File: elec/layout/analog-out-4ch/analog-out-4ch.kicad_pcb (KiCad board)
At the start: 2 copper layers, 15 parts, among them U1 240kΩ ±1% 62.5mW, U10 100nF ±10% 16V X7R, U2 33kΩ ±1% 62.5mW, U3 240kΩ ±1% 62.5mW, U4 33kΩ ±1% 62.5mW, U5 240kΩ ±1% 62.5mW, U6 33kΩ ±1% 62.5mW, U7 240kΩ ±1% 62.5mW, U8 33kΩ ±1% 62.5mW

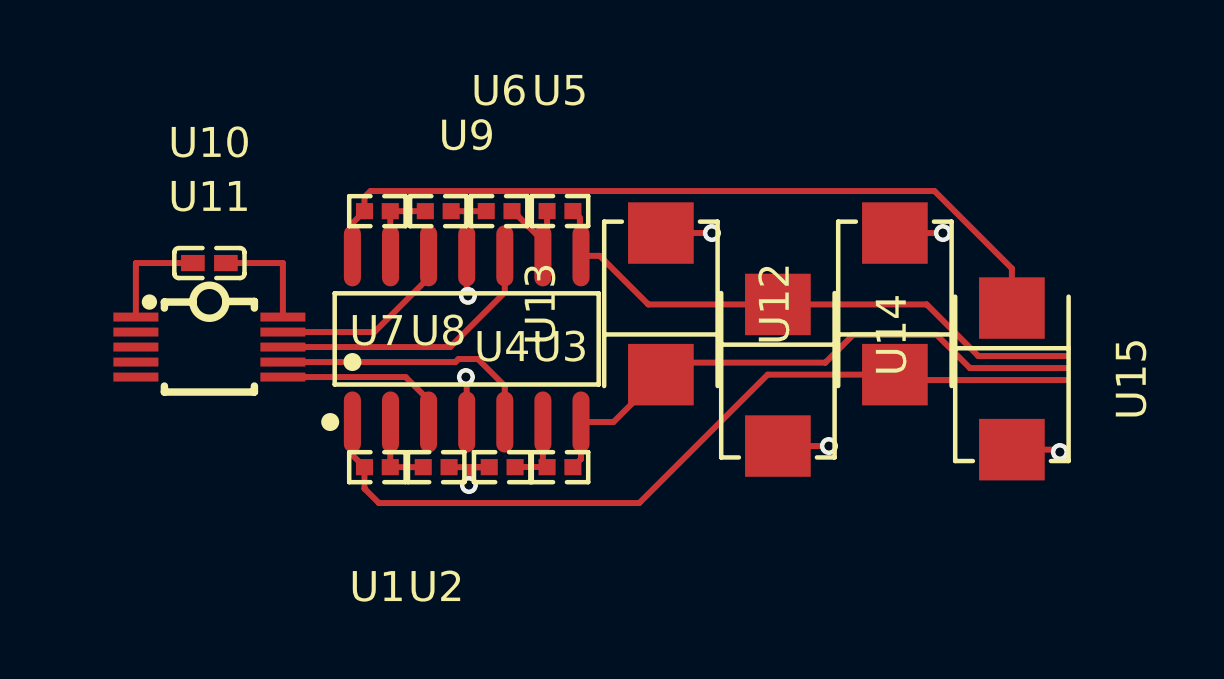
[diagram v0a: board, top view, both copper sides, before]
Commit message: fix short in thermistor design
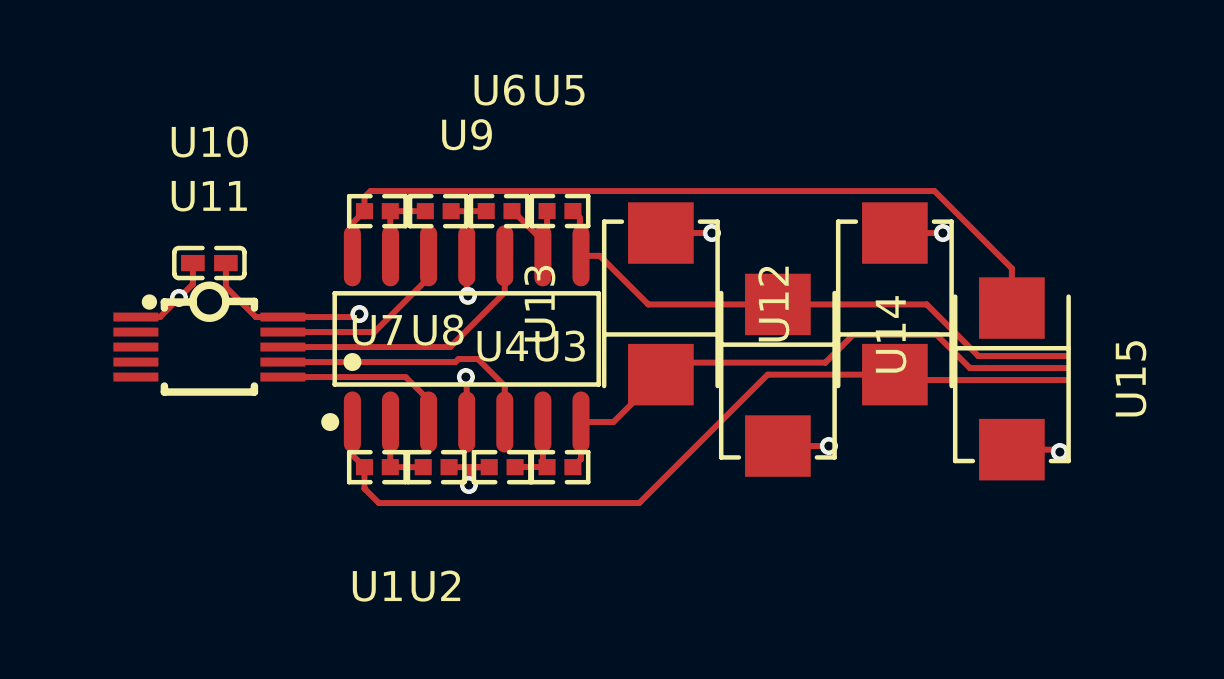
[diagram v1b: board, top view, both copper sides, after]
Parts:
- U1, U3, U5, U7: value 240kΩ ±1% 62.5mW -> 100Ω ±1% 62.5mW
- U2, U4, U6, U8: value 33kΩ ±1% 62.5mW -> 100Ω ±1% 62.5mW
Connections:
- U1 pad 2: line-4 -> line-6
- U10 pad 1: hv-1 -> hv
- U11 pad 1: hv-1 -> hv
- U11 pad 2: line-9 -> line-5
- U11 pad 6: line-7 -> line-9
- U11 pad 7: line-2 -> line-7
- U11 pad 8: line-6 -> line-4
- U11 pad 9: line-5 -> line-8
- U12 pad 1: line-4 -> line-6
- U12 pad 2: gnd-1 -> gnd
- U13 pad 1: line-1 -> line-2
- U13 pad 2: gnd-1 -> gnd
- U14 pad 1: line-8 -> line-1
- U14 pad 2: gnd-1 -> gnd
- U15 pad 2: gnd-1 -> gnd
- U2 pad 1: gnd-1 -> gnd
- U3 pad 2: line-1 -> line-2
- U4 pad 1: gnd-1 -> gnd
- U5 pad 2: line-8 -> line-1
- U6 pad 1: gnd-1 -> gnd
- U8 pad 1: gnd-1 -> gnd
- U9 pad 1: line-4 -> line-6
- U9 pad 10: line-6 -> line-4
- U9 pad 11: gnd-1 -> gnd
- U9 pad 12: line-5 -> line-8
- U9 pad 3: line-7 -> line-9
- U9 pad 4: hv -> hv-1
- U9 pad 5: line-2 -> line-7
- U9 pad 7: line-1 -> line-2
- U9 pad 8: line-8 -> line-1
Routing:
- net line-6: track 9.37 -> 28.3 mm
- net line-4: track 28.3 -> 9.37 mm
- net gnd: track 3.80 -> 20.6 mm, vias 0 -> 7
- net gnd-1: track 14.8 -> 0.00 mm, vias 6 -> 0
- net line-8: track 19.2 -> 6.34 mm
- net line-2: track 9.01 -> 19.9 mm
- net line-5: track 6.34 -> 0.00 mm
- net line-9: track 0.00 -> 5.91 mm
- net line-7: track 5.91 -> 9.01 mm
- net hv-1: track 3.70 -> 1.51 mm, vias 0 -> 1
- net hv: track 1.51 -> 3.06 mm
- net line-1: track 19.9 -> 19.2 mm

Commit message: update layouts to kicad 9
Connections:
- U1 pad 2: line-6 -> line-7
- U11 pad 2: line-5 -> line
- U11 pad 3: line -> line-2
- U11 pad 6: line-9 -> line-4
- U11 pad 7: line-7 -> line-6
- U11 pad 8: line-4 -> line-9
- U11 pad 9: line-8 -> line-1
- U12 pad 1: line-6 -> line-7
- U13 pad 1: line-2 -> line-3
- U14 pad 1: line-1 -> line-5
- U15 pad 1: line-3 -> line-8
- U3 pad 2: line-2 -> line-3
- U5 pad 2: line-1 -> line-5
- U7 pad 2: line-3 -> line-8
- U9 pad 1: line-6 -> line-7
- U9 pad 10: line-4 -> line-9
- U9 pad 12: line-8 -> line-1
- U9 pad 14: line-3 -> line-8
- U9 pad 3: line-9 -> line-4
- U9 pad 5: line-7 -> line-6
- U9 pad 7: line-2 -> line-3
- U9 pad 8: line-1 -> line-5
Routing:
- net line-8: track 6.34 -> 26.7 mm
- net line-2: track 19.9 -> 0.00 mm
- net line-7: track 9.01 -> 28.3 mm
- net line-6: track 28.3 -> 9.01 mm
- net line-5: track 0.00 -> 19.2 mm
- net line-1: track 19.2 -> 6.34 mm
- net line-3: track 26.7 -> 19.9 mm
- net line-9: track 5.91 -> 9.37 mm
- net line-4: track 9.37 -> 5.91 mm

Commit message: update LED gpio pin
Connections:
- U1 pad 2: line-7 -> line
- U11 pad 2: line -> line-2
- U11 pad 3: line-2 -> line-9
- U11 pad 6: line-4 -> line-3
- U11 pad 7: line-6 -> line-8
- U11 pad 8: line-9 -> line-5
- U12 pad 1: line-7 -> line
- U13 pad 1: line-3 -> line-4
- U14 pad 1: line-5 -> line-7
- U15 pad 1: line-8 -> line-6
- U3 pad 2: line-3 -> line-4
- U5 pad 2: line-5 -> line-7
- U7 pad 2: line-8 -> line-6
- U9 pad 1: line-7 -> line
- U9 pad 10: line-9 -> line-5
- U9 pad 14: line-8 -> line-6
- U9 pad 3: line-4 -> line-3
- U9 pad 5: line-6 -> line-8
- U9 pad 7: line-3 -> line-4
- U9 pad 8: line-5 -> line-7
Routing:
- net line: track 0.00 -> 28.3 mm
- net line-8: track 26.7 -> 9.01 mm
- net line-6: track 9.01 -> 26.7 mm
- net line-4: track 5.91 -> 19.9 mm
- net line-3: track 19.9 -> 5.91 mm
- net line-5: track 19.2 -> 9.37 mm
- net line-9: track 9.37 -> 0.00 mm
- net line-7: track 28.3 -> 19.2 mm
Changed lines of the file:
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@@
     )
     (net 0 "")
-    (net 1 "line-2")
-    (net 2 "line-4")
+    (net 1 "line-9")
+    (net 2 "line-3")
     (net 3 "hv")
     (net 4 "IN1_")
@@
     (net 7 "IN2_")
     (net 8 "IN3_")
-    (net 9 "line-6")
-    (net 10 "line-9")
+    (net 9 "line-8")
+    (net 10 "line-5")
     (net 11 "LDACh")
     (net 12 "RDY_BSYh")
-    (net 13 "line")
+    (net 13 "line-2")
     (net 14 "gnd")
-    (net 15 "line-3")
-    (net 16 "line-5")
-    (net 17 "line-8")
+    (net 15 "line-4")
+    (net 16 "line-7")
+    (net 17 "line-6")
     (net 18 "hv-1")
-    (net 19 "line-7")
+    (net 19 "line")
     (footprint "atopile:SMB_L4.6-W3.6-LS5.3-RD-330cb3"
         (layer "F.Cu")
@@
             (remove_unused_layers yes)
             (keep_end_layers yes)
-            (net 17 "line-8")
+            (net 17 "line-6")
         )
         (pad "2" smd rect
@@
             (remove_unused_layers yes)
             (keep_end_layers yes)
-            (net 16 "line-5")
+            (net 16 "line-7")
         )
         (pad "2" smd rect
@@
             (remove_unused_layers yes)
             (keep_end_layers yes)
-            (net 17 "line-8")
+            (net 17 "line-6")
         )
         (embedded_fonts no)
@@
             (remove_unused_layers yes)
             (keep_end_layers yes)
-            (net 16 "line-5")
+            (net 16 "line-7")
         )
         (embedded_fonts no)
@@
             (remove_unused_layers yes)
             (keep_end_layers yes)
-            (net 15 "line-3")
+            (net 15 "line-4")
         )
         (pad "2" smd rect
@@
             (remove_unused_layers yes)
             (keep_end_layers yes)
-            (net 19 "line-7")
+            (net 19 "line")
         )
         (embedded_fonts no)
@@
             (remove_unused_layers yes)
             (keep_end_layers yes)
-            (net 13 "line")
+            (net 13 "line-2")
         )
         (pad "3" smd rect
@@
             (remove_unused_layers yes)
             (keep_end_layers yes)
-            (net 1 "line-2")
+            (net 1 "line-9")
         )
         (pad "4" smd rect
@@
             (remove_unused_layers yes)
             (keep_end_layers yes)
-            (net 2 "line-4")
+            (net 2 "line-3")
         )
         (pad "7" smd rect
@@
             (remove_unused_layers yes)
             (keep_end_layers yes)
-            (net 9 "line-6")
+            (net 9 "line-8")
         )
         (pad "8" smd rect
@@
             (remove_unused_layers yes)
             (keep_end_layers yes)
-            (net 10 "line-9")
+            (net 10 "line-5")
         )
         (pad "9" smd rect
@@
             (remove_unused_layers yes)
             (keep_end_layers yes)
-            (net 15 "line-3")
+            (net 15 "line-4")
         )
         (embedded_fonts no)
@@
             (remove_unused_layers yes)
             (keep_end_layers yes)
-            (net 19 "line-7")
+            (net 19 "line")
         )
         (pad "2" smd oval
@@
             (remove_unused_layers yes)
             (keep_end_layers yes)
-            (net 2 "line-4")
+            (net 2 "line-3")
         )
         (pad "4" smd oval
@@
             (remove_unused_layers yes)
             (keep_end_layers yes)
-            (net 9 "line-6")
+            (net 9 "line-8")
         )
         (pad "6" smd oval
@@
             (remove_unused_layers yes)
             (keep_end_layers yes)
-            (net 15 "line-3")
+            (net 15 "line-4")
         )
         (pad "8" smd oval
@@
             (remove_unused_layers yes)
             (keep_end_layers yes)
-            (net 16 "line-5")
+            (net 16 "line-7")
         )
         (pad "9" smd oval
@@
             (remove_unused_layers yes)
             (keep_end_layers yes)
-            (net 10 "line-9")
+            (net 10 "line-5")
         )
         (pad "11" smd oval
@@
             (remove_unused_layers yes)
             (keep_end_layers yes)
-            (net 17 "line-8")
+            (net 17 "line-6")
         )
         (embedded_fonts no)
@@
             (remove_unused_layers yes)
             (keep_end_layers yes)
-            (net 19 "line-7")
+            (net 19 "line")
         )
         (pad "2" smd rect

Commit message: restore layout files
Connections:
- U11 pad 2: line-2 -> line-4
- U11 pad 3: line-9 -> line-2
- U11 pad 6: line-3 -> line-8
- U11 pad 7: line-8 -> line-6
- U11 pad 9: line-1 -> line-7
- U13 pad 1: line-4 -> line-3
- U14 pad 1: line-7 -> line-1
- U15 pad 1: line-6 -> line-9
- U3 pad 2: line-4 -> line-3
- U5 pad 2: line-7 -> line-1
- U7 pad 2: line-6 -> line-9
- U9 pad 12: line-1 -> line-7
- U9 pad 14: line-6 -> line-9
- U9 pad 3: line-3 -> line-8
- U9 pad 5: line-8 -> line-6
- U9 pad 7: line-4 -> line-3
- U9 pad 8: line-7 -> line-1
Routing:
- net line-9: track 0.00 -> 26.7 mm
- net line-4: track 19.9 -> 0.00 mm
- net line-6: track 26.7 -> 9.01 mm
- net line-3: track 5.91 -> 19.9 mm
- net line-7: track 19.2 -> 6.34 mm
- net line-1: track 6.34 -> 19.2 mm
- net line-8: track 9.01 -> 5.91 mm

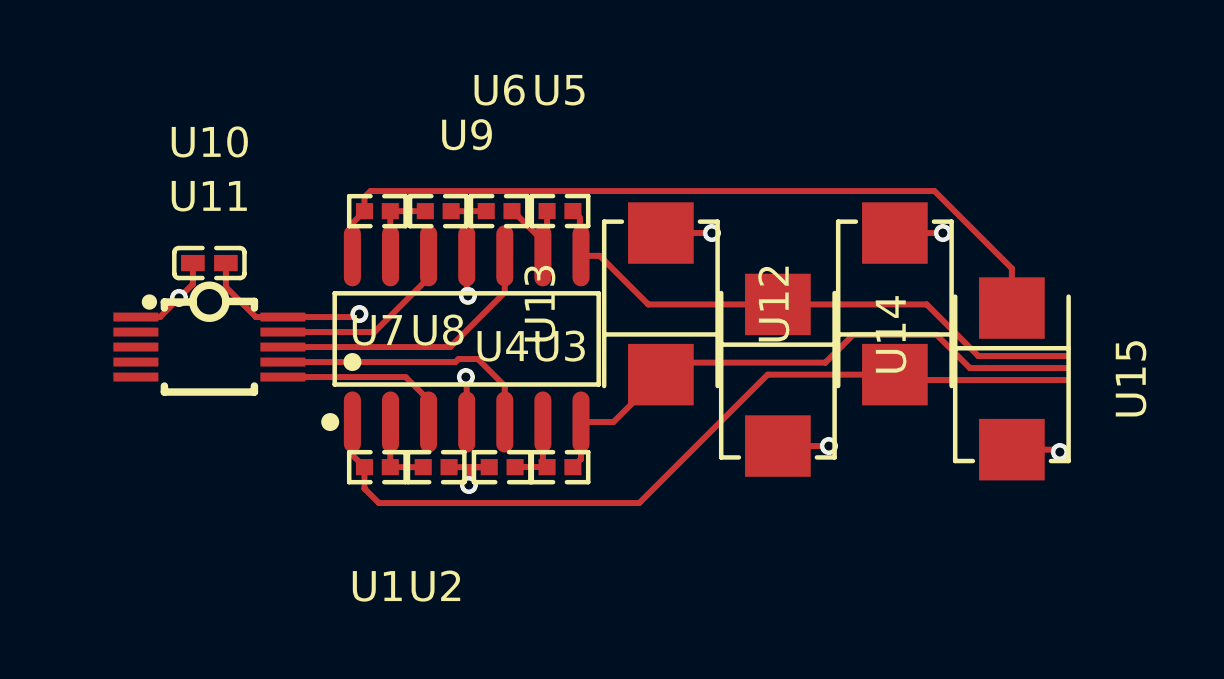
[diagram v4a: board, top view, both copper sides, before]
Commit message: add power button and boot button, fix CAN layout
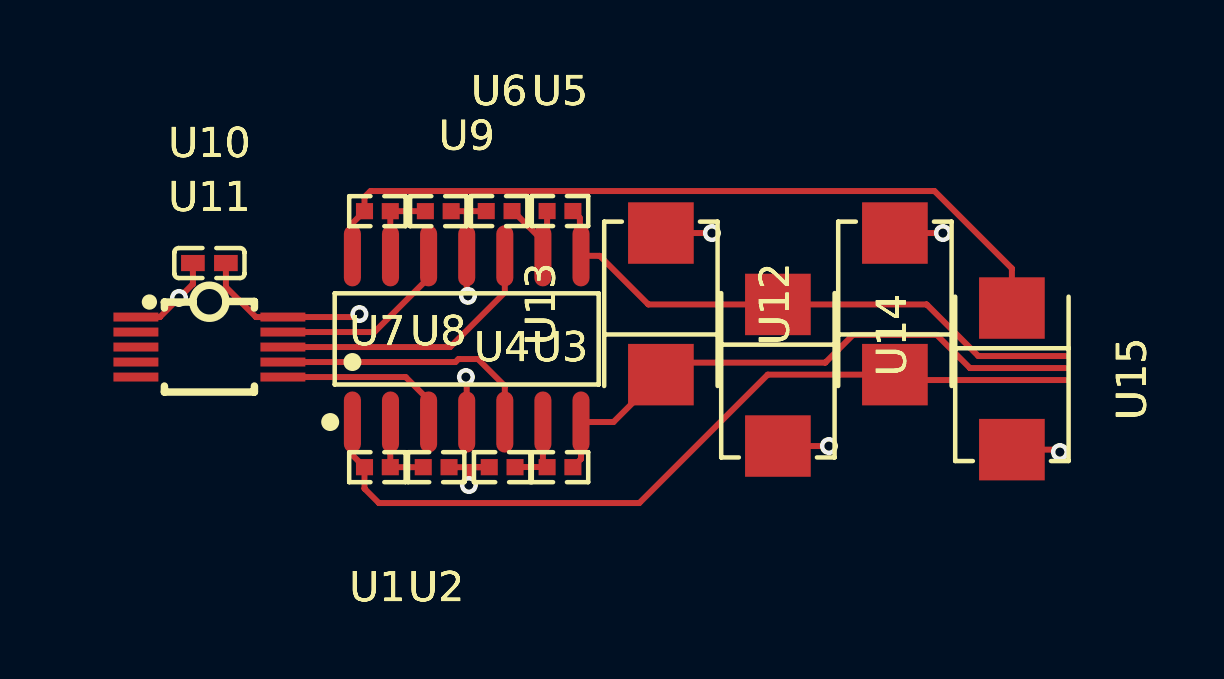
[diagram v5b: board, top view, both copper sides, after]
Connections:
- U1 pad 2: line -> line-5
- U10 pad 1: hv -> hv-1
- U11 pad 1: hv -> hv-1
- U11 pad 2: line-4 -> line-1
- U11 pad 3: line-2 -> line-8
- U11 pad 6: line-8 -> line-2
- U11 pad 7: line-6 -> line
- U11 pad 8: line-5 -> line-4
- U11 pad 9: line-7 -> line-3
- U12 pad 1: line -> line-5
- U13 pad 1: line-3 -> line-9
- U14 pad 1: line-1 -> line-7
- U15 pad 1: line-9 -> line-6
- U3 pad 2: line-3 -> line-9
- U5 pad 2: line-1 -> line-7
- U7 pad 2: line-9 -> line-6
- U9 pad 1: line -> line-5
- U9 pad 10: line-5 -> line-4
- U9 pad 12: line-7 -> line-3
- U9 pad 14: line-9 -> line-6
- U9 pad 3: line-8 -> line-2
- U9 pad 4: hv-1 -> hv
- U9 pad 5: line-6 -> line
- U9 pad 7: line-3 -> line-9
- U9 pad 8: line-1 -> line-7
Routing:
- net line: track 28.3 -> 9.01 mm
- net line-1: track 19.2 -> 0.00 mm
- net line-5: track 9.37 -> 28.3 mm
- net line-6: track 9.01 -> 26.7 mm
- net line-3: track 19.9 -> 6.34 mm
- net line-7: track 6.34 -> 19.2 mm
- net line-4: track 0.00 -> 9.37 mm
- net line-9: track 26.7 -> 19.9 mm
- net line-8: track 5.91 -> 0.00 mm
- net line-2: track 0.00 -> 5.91 mm
- net hv-1: track 1.51 -> 3.06 mm
- net hv: track 3.06 -> 1.51 mm

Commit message: Cleanup layout
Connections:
- U1 pad 2: line-5 -> line-6
- U11 pad 2: line-1 -> line-7
- U11 pad 3: line-8 -> line-9
- U11 pad 6: line-2 -> line
- U11 pad 7: line -> line-5
- U11 pad 9: line-3 -> line-8
- U12 pad 1: line-5 -> line-6
- U13 pad 1: line-9 -> line-1
- U14 pad 1: line-7 -> line-2
- U15 pad 1: line-6 -> line-3
- U3 pad 2: line-9 -> line-1
- U5 pad 2: line-7 -> line-2
- U7 pad 2: line-6 -> line-3
- U9 pad 1: line-5 -> line-6
- U9 pad 12: line-3 -> line-8
- U9 pad 14: line-6 -> line-3
- U9 pad 3: line-2 -> line
- U9 pad 5: line -> line-5
- U9 pad 7: line-9 -> line-1
- U9 pad 8: line-7 -> line-2
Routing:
- net line-3: track 6.34 -> 26.7 mm
- net line-9: track 19.9 -> 0.00 mm
- net line-1: track 0.00 -> 19.9 mm
- net line-5: track 28.3 -> 9.01 mm
- net line-7: track 19.2 -> 0.00 mm
- net line-2: track 5.91 -> 19.2 mm
- net line-8: track 0.00 -> 6.34 mm
- net line: track 9.01 -> 5.91 mm
- net line-6: track 26.7 -> 28.3 mm
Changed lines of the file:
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@@
 	)
 	(net 0 "")
-	(net 1 "line-8")
-	(net 2 "line-2")
+	(net 1 "line-9")
+	(net 2 "line")
 	(net 3 "hv-1")
 	(net 4 "IN1_")
-	(net 5 "line-3")
+	(net 5 "line-8")
 	(net 6 "IN4_")
 	(net 7 "IN2_")
 	(net 8 "IN3_")
-	(net 9 "line")
+	(net 9 "line-5")
 	(net 10 "line-4")
 	(net 11 "LDACh")
 	(net 12 "RDY_BSYh")
-	(net 13 "line-1")
+	(net 13 "line-7")
 	(net 14 "gnd")
-	(net 15 "line-9")
-	(net 16 "line-7")
-	(net 17 "line-6")
+	(net 15 "line-1")
+	(net 16 "line-2")
+	(net 17 "line-3")
 	(net 18 "hv")
-	(net 19 "line-5")
+	(net 19 "line-6")
 	(footprint "atopile:SMB_L4.6-W3.6-LS5.3-RD-330cb3"
 		(layer "F.Cu")
@@
 			(size 2.05 2.19)
 			(layers "F.Cu" "F.Mask" "F.Paste")
-			(net 17 "line-6")
+			(net 17 "line-3")
 		)
 		(pad "2" smd rect
@@
 			(size 2.05 2.19)
 			(layers "F.Cu" "F.Mask" "F.Paste")
-			(net 16 "line-7")
+			(net 16 "line-2")
 		)
 		(pad "2" smd rect
@@
 			(size 0.57 0.54)
 			(layers "F.Cu" "F.Mask" "F.Paste")
-			(net 17 "line-6")
+			(net 17 "line-3")
 		)
 		(embedded_fonts no)
@@
 			(size 0.57 0.54)
 			(layers "F.Cu" "F.Mask" "F.Paste")
-			(net 16 "line-7")
+			(net 16 "line-2")
 		)
 		(embedded_fonts no)
@@
 			(size 2.05 2.19)
 			(layers "F.Cu" "F.Mask" "F.Paste")
-			(net 15 "line-9")
+			(net 15 "line-1")
 		)
 		(pad "2" smd rect
@@
 			(size 0.57 0.54)
 			(layers "F.Cu" "F.Mask" "F.Paste")
-			(net 19 "line-5")
+			(net 19 "line-6")
 		)
 		(embedded_fonts no)
@@
 			(size 1.5 0.3)
 			(layers "F.Cu" "F.Mask" "F.Paste")
-			(net 13 "line-1")
+			(net 13 "line-7")
 		)
 		(pad "3" smd rect
@@
 			(size 1.5 0.3)
 			(layers "F.Cu" "F.Mask" "F.Paste")
-			(net 1 "line-8")
+			(net 1 "line-9")
 		)
 		(pad "4" smd rect
@@
 			(size 1.5 0.3)
 			(layers "F.Cu" "F.Mask" "F.Paste")
-			(net 2 "line-2")
+			(net 2 "line")
 		)
 		(pad "7" smd rect
@@
 			(size 1.5 0.3)
 			(layers "F.Cu" "F.Mask" "F.Paste")
-			(net 9 "line")
+			(net 9 "line-5")
 		)
 		(pad "8" smd rect
@@
 			(size 1.5 0.3)
 			(layers "F.Cu" "F.Mask" "F.Paste")
-			(net 5 "line-3")
+			(net 5 "line-8")
 		)
 		(pad "10" smd rect
@@
 			(size 0.57 0.54)
 			(layers "F.Cu" "F.Mask" "F.Paste")
-			(net 15 "line-9")
+			(net 15 "line-1")
 		)
 		(embedded_fonts no)
@@
 			(size 0.57 2.04)
 			(layers "F.Cu" "F.Mask" "F.Paste")
-			(net 19 "line-5")
+			(net 19 "line-6")
 		)
 		(pad "2" smd oval
@@
 			(size 0.57 2.04)
 			(layers "F.Cu" "F.Mask" "F.Paste")
-			(net 2 "line-2")
+			(net 2 "line")
 		)
 		(pad "4" smd oval
@@
 			(size 0.57 2.04)
 			(layers "F.Cu" "F.Mask" "F.Paste")
-			(net 9 "line")
+			(net 9 "line-5")
 		)
 		(pad "6" smd oval
@@
 			(size 0.57 2.04)
 			(layers "F.Cu" "F.Mask" "F.Paste")
-			(net 15 "line-9")
+			(net 15 "line-1")
 		)
 		(pad "8" smd oval
@@
 			(size 0.57 2.04)
 			(layers "F.Cu" "F.Mask" "F.Paste")
-			(net 16 "line-7")
+			(net 16 "line-2")
 		)
 		(pad "9" smd oval
@@
 			(size 0.57 2.04)
 			(layers "F.Cu" "F.Mask" "F.Paste")
-			(net 5 "line-3")
+			(net 5 "line-8")
 		)
 		(pad "13" smd oval
@@
 			(size 0.57 2.04)
 			(layers "F.Cu" "F.Mask" "F.Paste")
-			(net 17 "line-6")
+			(net 17 "line-3")
 		)
 		(embedded_fonts no)
@@
 			(size 2.05 2.19)
 			(layers "F.Cu" "F.Mask" "F.Paste")
-			(net 19 "line-5")
+			(net 19 "line-6")
 		)
 		(pad "2" smd rect
